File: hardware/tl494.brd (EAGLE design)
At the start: 100 x 80 mm, 87 parts, among them IC1 TL494CN, J1 CON_HEADER_1X02-PTH, J2 CON_HEADER_1X02-PTH, J3 J20MM, J4 J5MM, J5 J15MM, K2 24V, Q1 2N5551, Q1I 8050, Q1I1 2N3904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

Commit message: updated the board
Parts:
- added H3, H4, H5: HEATSINK1, trosh_devices.eagle.v9:TO-220_HEATSINK1
- added Q5: TIP31, trosh_devices.eagle.v9:TO-220V
- D10: value 15V 1/2W -> 16V 1/4W
- D2: device diode:DO41-10 -> trosh_devices.eagle.v9:RAD2,5_EXPAD
- D4: device diode:DO35-10 -> trosh_devices.eagle.v9:DO35-20
- R15, R30, R31, R7, R8: device trosh_devices.eagle.v9:0207/10_EXPAD -> trosh_devices.eagle.v9:0207/2V_EXPAD
- R33: value 4K 2W -> 100K; device trosh_devices.eagle.v9:0414V_EXPAD -> trosh_devices.eagle.v9:0207/2V_EXPAD
- moved C16 10.2 mm to (33.0, 35.6)
- moved R33 9.92 mm to (40.6, 26.7), turned to 180 degrees
- moved D10 4.58 mm to (36.8, 30.5)
- moved R7 3.81 mm to (27.9, 50.8)
- moved R8 3.81 mm to (27.9, 48.3)
- moved C9 3.70 mm to (51.4, 51.4), turned to 180 degrees
- moved J3 3.18 mm to (55.9, 57.8)
- moved R31 2.84 mm to (29.2, 30.5), turned to 0 degrees
- moved R15 2.84 mm to (17.8, 22.9)
- moved D4 2.84 mm to (75.6, 55.9)
- moved R16 2.54 mm to (50.2, 24.1)
- moved C6 2.54 mm to (22.9, 27.9)
- moved C8 2.54 mm to (59.7, 31.8)
- moved D2 2.29 mm to (65.4, 25.4), turned to 0 degrees
- moved C10 1.91 mm to (65.4, 53.3)
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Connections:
- new net N$39: D10.C, Q5.1, R33.2
- net +15V: now also Q5.3; no longer D10.C, R33.2
- net +V: now also Q5.2
- net N$16: now also R17.2; no longer R17.1
- net N$17: now also R17.1; no longer R17.2
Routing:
- net N$9: track 39.9 -> 29.7 mm
- net N$39: track 0.00 -> 8.89 mm
- net VOUT: track 164.3 -> 156.0 mm
- net +V: track 46.9 -> 53.8 mm
- net N$15: track 22.4 -> 16.7 mm
- net N$10: track 16.8 -> 13.5 mm
- net N$13: track 19.4 -> 21.6 mm
- net N$27: track 15.7 -> 14.1 mm
- net N$21: track 5.08 -> 6.35 mm
- net N$16: track 29.4 -> 28.2 mm

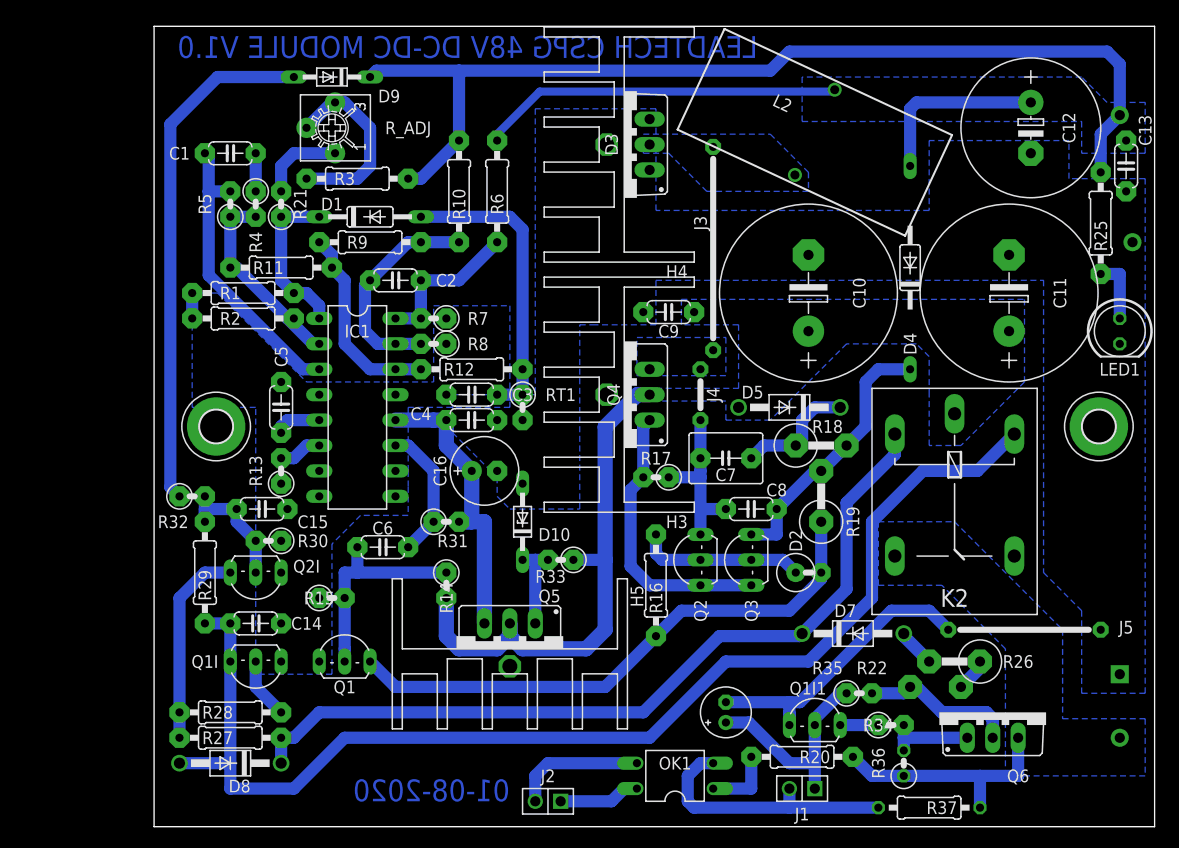
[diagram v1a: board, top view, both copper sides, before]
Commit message: added measured values on schematic
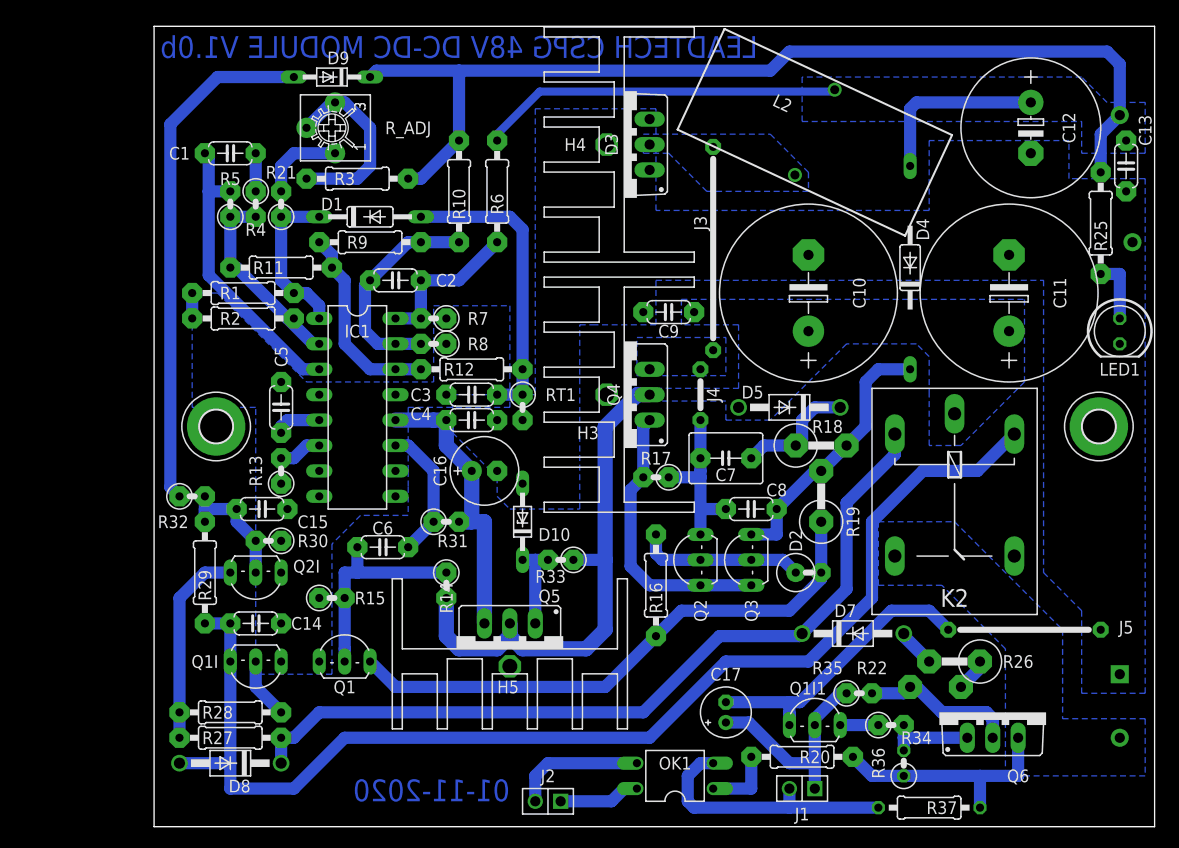
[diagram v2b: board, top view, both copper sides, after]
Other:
- board text added: "01-11-2020"
- board text added: "LEADTECH CSPG 48V DC-DC MODULE V1.0b"
- board text removed: "01-08-2020"
- board text removed: "LEADTECH CSPG 48V DC-DC MODULE V1.0"
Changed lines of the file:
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@@
 <?xml version="1.0" encoding="utf-8"?>
 <!DOCTYPE eagle SYSTEM "eagle.dtd">
-<eagle version="9.1.3">
+<eagle version="9.4.2">
 <drawing>
 <settings>
@@
 <grid distance="50" unitdist="mil" unit="mil" style="lines" multiple="1" display="no" altdistance="25" altunitdist="mil" altunit="mil"/>
 <layers>
-<layer number="1" name="Top" color="4" fill="1" visible="yes" active="yes"/>
+<layer number="1" name="Top" color="4" fill="1" visible="no" active="yes"/>
 <layer number="2" name="Route2" color="1" fill="3" visible="no" active="no"/>
 <layer number="15" name="Route15" color="4" fill="6" visible="no" active="no"/>
-<layer number="16" name="Bottom" color="1" fill="1" visible="yes" active="yes"/>
-<layer number="17" name="Pads" color="2" fill="1" visible="yes" active="yes"/>
+<layer number="16" name="Bottom" color="1" fill="1" visible="no" active="yes"/>
+<layer number="17" name="Pads" color="2" fill="1" visible="no" active="yes"/>
 <layer number="18" name="Vias" color="2" fill="1" visible="yes" active="yes"/>
 <layer number="19" name="Unrouted" color="6" fill="1" visible="yes" active="yes"/>
@@
 <layer number="21" name="tPlace" color="7" fill="1" visible="yes" active="yes"/>
 <layer number="22" name="bPlace" color="7" fill="1" visible="yes" active="yes"/>
-<layer number="23" name="tOrigins" color="15" fill="1" visible="yes" active="yes"/>
-<layer number="24" name="bOrigins" color="15" fill="1" visible="yes" active="yes"/>
+<layer number="23" name="tOrigins" color="15" fill="1" visible="no" active="yes"/>
+<layer number="24" name="bOrigins" color="15" fill="1" visible="no" active="yes"/>
 <layer number="25" name="tNames" color="7" fill="1" visible="yes" active="yes"/>
 <layer number="26" name="bNames" color="7" fill="1" visible="yes" active="yes"/>
@@
 <layer number="37" name="tTest" color="7" fill="1" visible="no" active="yes"/>
 <layer number="38" name="bTest" color="7" fill="1" visible="no" active="yes"/>
-<layer number="39" name="tKeepout" color="4" fill="11" visible="yes" active="yes"/>
-<layer number="40" name="bKeepout" color="1" fill="11" visible="yes" active="yes"/>
-<layer number="41" name="tRestrict" color="4" fill="10" visible="yes" active="yes"/>
-<layer number="42" name="bRestrict" color="1" fill="10" visible="yes" active="yes"/>
+<layer number="39" name="tKeepout" color="4" fill="11" visible="no" active="yes"/>
+<layer number="40" name="bKeepout" color="1" fill="11" visible="no" active="yes"/>
+<layer number="41" name="tRestrict" color="4" fill="10" visible="no" active="yes"/>
+<layer number="42" name="bRestrict" color="1" fill="10" visible="no" active="yes"/>
 <layer number="43" name="vRestrict" color="2" fill="10" visible="no" active="yes"/>
 <layer number="44" name="Drills" color="7" fill="1" visible="no" active="yes"/>
@@
 <wire x1="100" y1="80" x2="0" y2="80" width="0" layer="20"/>
 <wire x1="0" y1="80" x2="0" y2="0" width="0" layer="20"/>
-<text x="35.56" y="2.54" size="2.1844" layer="16" font="vector" ratio="18" rot="MR0">01-08-2020</text>
-<text x="60.325" y="76.835" size="2.1844" layer="16" font="vector" ratio="18" rot="MR0">LEADTECH CSPG 48V DC-DC MODULE V1.0</text>
+<text x="35.56" y="2.54" size="2.1844" layer="16" font="vector" ratio="18" rot="MR0">01-11-2020</text>
+<text x="60.325" y="76.835" size="2.1844" layer="16" font="vector" ratio="18" rot="MR0">LEADTECH CSPG 48V DC-DC MODULE V1.0b</text>
 </plain>
 <attributes>
@@
 </element>
 <element name="C3" library="trosh_devices.eagle.v9" package="C050-024X044_EXPAD" value="0.1uF" x="31.75" y="43.18" smashed="yes">
-<attribute name="NAME" x="36.83" y="43.18" size="1.27" layer="25" ratio="10" align="center"/>
+<attribute name="NAME" x="26.67" y="43.18" size="1.27" layer="25" ratio="10" align="center"/>
 <attribute name="VALUE" x="28.194" y="40.132" size="1.27" layer="27" ratio="10"/>
 </element>
@@
 </element>
 <element name="D4" library="trosh_devices.eagle.v9" package="DO35-20" value="1N4148" x="75.565" y="55.88" smashed="yes" rot="R90">
-<attribute name="NAME" x="75.565" y="48.26" size="1.27" layer="25" ratio="10" rot="R90" align="center"/>
+<attribute name="NAME" x="76.835" y="59.69" size="1.27" layer="25" ratio="10" rot="R90" align="center"/>
 <attribute name="VALUE" x="78.232" y="53.721" size="1.27" layer="27" ratio="10" rot="R90"/>
 </element>
@@
 </element>
 <element name="D9" library="diode" library_urn="urn:adsk.eagle:library:210" package="DO34Z7" package3d_urn="urn:adsk.eagle:package:43364/1" value="15V 1/2W" x="17.78" y="74.93" smashed="yes" rot="R180">
-<attribute name="NAME" x="23.495" y="73.025" size="1.27" layer="25" ratio="10" rot="R180" align="center"/>
+<attribute name="NAME" x="18.415" y="76.835" size="1.27" layer="25" ratio="10" rot="R180" align="center"/>
 <attribute name="POPULARITY" value="1" x="-55.88" y="129.54" size="1.778" layer="27" rot="R180" display="off"/>
 <attribute name="VALUE" x="19.304" y="77.343" size="1.27" layer="27" ratio="10" rot="R180"/>
@@
 </element>
 <element name="R15" library="trosh_devices.eagle.v9" package="0207/2V_EXPAD" value="4.7K" x="17.78" y="22.86" smashed="yes">
-<attribute name="NAME" x="16.51" y="22.86" size="1.27" layer="25" ratio="10" align="center"/>
+<attribute name="NAME" x="21.59" y="22.86" size="1.27" layer="25" ratio="10" align="center"/>
 <attribute name="VALUE" x="15.5194" y="22.225" size="1.27" layer="27" ratio="10"/>
 </element>
@@
 </element>
 <element name="R21" library="trosh_devices.eagle.v9" package="0207/2V_EXPAD" value="5.6K" x="12.7" y="62.23" smashed="yes" rot="R90">
-<attribute name="NAME" x="14.605" y="62.23" size="1.27" layer="25" ratio="10" rot="R90" align="center"/>
+<attribute name="NAME" x="12.7" y="65.405" size="1.27" layer="25" ratio="10" rot="R180" align="center"/>
 <attribute name="VALUE" x="13.335" y="59.9694" size="1.27" layer="27" ratio="10" rot="R90"/>
 </element>
@@
 </element>
 <element name="R4" library="trosh_devices.eagle.v9" package="0207/2V_EXPAD" value="10K" x="10.16" y="62.23" smashed="yes" rot="R270">
-<attribute name="NAME" x="10.16" y="58.42" size="1.27" layer="25" ratio="10" rot="R270" align="center"/>
+<attribute name="NAME" x="10.16" y="59.69" size="1.27" layer="25" ratio="10" align="center"/>
 <attribute name="VALUE" x="9.525" y="64.4906" size="1.27" layer="27" ratio="10" rot="R270"/>
 </element>
 <element name="R5" library="trosh_devices.eagle.v9" package="0207/2V_EXPAD" value="470K" x="7.62" y="62.23" smashed="yes" rot="R90">
-<attribute name="NAME" x="5.08" y="62.23" size="1.27" layer="25" ratio="10" rot="R90" align="center"/>
+<attribute name="NAME" x="7.62" y="64.77" size="1.27" layer="25" ratio="10" align="center"/>
 <attribute name="VALUE" x="8.255" y="59.9694" size="1.27" layer="27" ratio="10" rot="R90"/>
 </element>
@@
 </element>
 <element name="R34" library="trosh_devices.eagle.v9" package="0207/2V_EXPAD" value="50K" x="73.66" y="10.16" smashed="yes">
-<attribute name="NAME" x="72.39" y="10.16" size="1.27" layer="25" ratio="10" align="center"/>
+<attribute name="NAME" x="76.2" y="8.89" size="1.27" layer="25" ratio="10" align="center"/>
 <attribute name="VALUE" x="71.3994" y="9.525" size="1.27" layer="27" ratio="10"/>
 </element>
@@
 </element>
 <element name="C17" library="trosh_devices.eagle.v9" package="E2-5_EXPAD" value="1uF 63V" x="57.15" y="11.43" smashed="yes" rot="R90">
-<attribute name="NAME" x="52.07" y="11.43" size="1.27" layer="26" ratio="10" rot="MR0" align="center"/>
+<attribute name="NAME" x="57.15" y="15.24" size="1.27" layer="25" ratio="10" align="center"/>
 <attribute name="VALUE" x="60.198" y="8.128" size="1.27" layer="27" ratio="10" rot="R90"/>
 </element>
@@
 <attribute name="VALUE" x="60.630865625" y="69.820384375" size="1.27" layer="27" rot="R335"/>
 </element>
-<element name="H3" library="trosh_devices.eagle.v9" package="TO-220_HEATSINK1" value="HEATSINK1" x="46.99" y="43.18" rot="R90"/>
-<element name="H4" library="trosh_devices.eagle.v9" package="TO-220_HEATSINK1" value="HEATSINK1" x="46.99" y="68.18" rot="R90"/>
-<element name="H5" library="trosh_devices.eagle.v9" package="TO-220_HEATSINK1" value="HEATSINK1" x="35.56" y="17.78" rot="R180"/>
-<element name="Q5" library="trosh_devices.eagle.v9" package="TO-220V" value="TIP31" x="35.56" y="20.32" rot="R180"/>
+<element name="H3" library="trosh_devices.eagle.v9" package="TO-220_HEATSINK1" value="HEATSINK1" x="46.99" y="43.18" smashed="yes" rot="R90">
+<attribute name="NAME" x="44.45" y="40.005" size="1.27" layer="25" font="vector" ratio="10" rot="R180"/>
+<attribute name="VALUE" x="53.34" y="56.515" size="1.27" layer="27" ratio="10" rot="R180"/>
+</element>
+<element name="H4" library="trosh_devices.eagle.v9" package="TO-220_HEATSINK1" value="HEATSINK1" x="46.99" y="68.18" smashed="yes" rot="R90">
+<attribute name="NAME" x="43.18" y="68.815" size="1.27" layer="25" font="vector" ratio="10" rot="R180"/>
+<attribute name="VALUE" x="53.34" y="81.515" size="1.27" layer="27" ratio="10" rot="R180"/>
+</element>
+<element name="H5" library="trosh_devices.eagle.v9" package="TO-220_HEATSINK1" value="HEATSINK1" x="35.56" y="17.78" smashed="yes" rot="R180">
+<attribute name="NAME" x="34.29" y="13.335" size="1.27" layer="25" font="vector" ratio="10"/>
+<attribute name="VALUE" x="22.225" y="24.13" size="1.27" layer="27" ratio="10" rot="R270"/>
+</element>
+<element name="Q5" library="trosh_devices.eagle.v9" package="TO-220V" value="TIP31" x="35.56" y="20.32" smashed="yes" rot="R180">
+<attribute name="NAME" x="40.64" y="23.6982" size="1.27" layer="25" font="vector" ratio="10" rot="R180"/>
+<attribute name="VALUE" x="40.64" y="25.4" size="1.27" layer="27" font="vector" ratio="10" rot="R180"/>
+</element>
 </elements>
 <signals>

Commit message: schematic tiny updates
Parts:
- R14: value 68K -> 130K
- R15: value 4.7K -> 4.3K
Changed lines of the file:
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@@
 <grid distance="50" unitdist="mil" unit="mil" style="lines" multiple="1" display="no" altdistance="25" altunitdist="mil" altunit="mil"/>
 <layers>
-<layer number="1" name="Top" color="4" fill="1" visible="no" active="yes"/>
+<layer number="1" name="Top" color="4" fill="1" visible="yes" active="yes"/>
 <layer number="2" name="Route2" color="1" fill="3" visible="no" active="no"/>
 <layer number="15" name="Route15" color="4" fill="6" visible="no" active="no"/>
-<layer number="16" name="Bottom" color="1" fill="1" visible="no" active="yes"/>
-<layer number="17" name="Pads" color="2" fill="1" visible="no" active="yes"/>
+<layer number="16" name="Bottom" color="1" fill="1" visible="yes" active="yes"/>
+<layer number="17" name="Pads" color="2" fill="1" visible="yes" active="yes"/>
 <layer number="18" name="Vias" color="2" fill="1" visible="yes" active="yes"/>
 <layer number="19" name="Unrouted" color="6" fill="1" visible="yes" active="yes"/>
@@
 <layer number="21" name="tPlace" color="7" fill="1" visible="yes" active="yes"/>
 <layer number="22" name="bPlace" color="7" fill="1" visible="yes" active="yes"/>
-<layer number="23" name="tOrigins" color="15" fill="1" visible="no" active="yes"/>
-<layer number="24" name="bOrigins" color="15" fill="1" visible="no" active="yes"/>
+<layer number="23" name="tOrigins" color="15" fill="1" visible="yes" active="yes"/>
+<layer number="24" name="bOrigins" color="15" fill="1" visible="yes" active="yes"/>
 <layer number="25" name="tNames" color="7" fill="1" visible="yes" active="yes"/>
 <layer number="26" name="bNames" color="7" fill="1" visible="yes" active="yes"/>
@@
 <layer number="37" name="tTest" color="7" fill="1" visible="no" active="yes"/>
 <layer number="38" name="bTest" color="7" fill="1" visible="no" active="yes"/>
-<layer number="39" name="tKeepout" color="4" fill="11" visible="no" active="yes"/>
-<layer number="40" name="bKeepout" color="1" fill="11" visible="no" active="yes"/>
-<layer number="41" name="tRestrict" color="4" fill="10" visible="no" active="yes"/>
-<layer number="42" name="bRestrict" color="1" fill="10" visible="no" active="yes"/>
+<layer number="39" name="tKeepout" color="4" fill="11" visible="yes" active="yes"/>
+<layer number="40" name="bKeepout" color="1" fill="11" visible="yes" active="yes"/>
+<layer number="41" name="tRestrict" color="4" fill="10" visible="yes" active="yes"/>
+<layer number="42" name="bRestrict" color="1" fill="10" visible="yes" active="yes"/>
 <layer number="43" name="vRestrict" color="2" fill="10" visible="no" active="yes"/>
 <layer number="44" name="Drills" color="7" fill="1" visible="no" active="yes"/>
@@
 <attribute name="VALUE" x="13.335" y="33.2994" size="1.27" layer="27" ratio="10" rot="R90"/>
 </element>
-<element name="R14" library="trosh_devices.eagle.v9" package="0207/2V_EXPAD" value="68K" x="29.21" y="24.13" smashed="yes" rot="R270">
+<element name="R14" library="trosh_devices.eagle.v9" package="0207/2V_EXPAD" value="130K" x="29.21" y="24.13" smashed="yes" rot="R270">
 <attribute name="NAME" x="29.21" y="22.86" size="1.27" layer="25" ratio="10" rot="R270" align="center"/>
 <attribute name="VALUE" x="28.575" y="26.3906" size="1.27" layer="27" ratio="10" rot="R270"/>
 </element>
-<element name="R15" library="trosh_devices.eagle.v9" package="0207/2V_EXPAD" value="4.7K" x="17.78" y="22.86" smashed="yes">
+<element name="R15" library="trosh_devices.eagle.v9" package="0207/2V_EXPAD" value="4.3K" x="17.78" y="22.86" smashed="yes">
 <attribute name="NAME" x="21.59" y="22.86" size="1.27" layer="25" ratio="10" align="center"/>
 <attribute name="VALUE" x="15.5194" y="22.225" size="1.27" layer="27" ratio="10"/>

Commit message: 1
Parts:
- R15: value 4.3K -> 4.7K
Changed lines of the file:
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@@
 <layer number="37" name="tTest" color="7" fill="1" visible="no" active="yes"/>
 <layer number="38" name="bTest" color="7" fill="1" visible="no" active="yes"/>
-<layer number="39" name="tKeepout" color="4" fill="11" visible="yes" active="yes"/>
+<layer number="39" name="tKeepout" color="4" fill="11" visible="no" active="yes"/>
 <layer number="40" name="bKeepout" color="1" fill="11" visible="yes" active="yes"/>
 <layer number="41" name="tRestrict" color="4" fill="10" visible="yes" active="yes"/>
@@
 <attribute name="VALUE" x="28.575" y="26.3906" size="1.27" layer="27" ratio="10" rot="R270"/>
 </element>
-<element name="R15" library="trosh_devices.eagle.v9" package="0207/2V_EXPAD" value="4.3K" x="17.78" y="22.86" smashed="yes">
+<element name="R15" library="trosh_devices.eagle.v9" package="0207/2V_EXPAD" value="4.7K" x="17.78" y="22.86" smashed="yes">
 <attribute name="NAME" x="21.59" y="22.86" size="1.27" layer="25" ratio="10" align="center"/>
 <attribute name="VALUE" x="15.5194" y="22.225" size="1.27" layer="27" ratio="10"/>
